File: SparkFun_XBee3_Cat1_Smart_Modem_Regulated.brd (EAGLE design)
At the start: 33 x 52.1 mm, 95 parts, among them J4 QWIIC_RIGHT_ANGLE, U2 AP63203

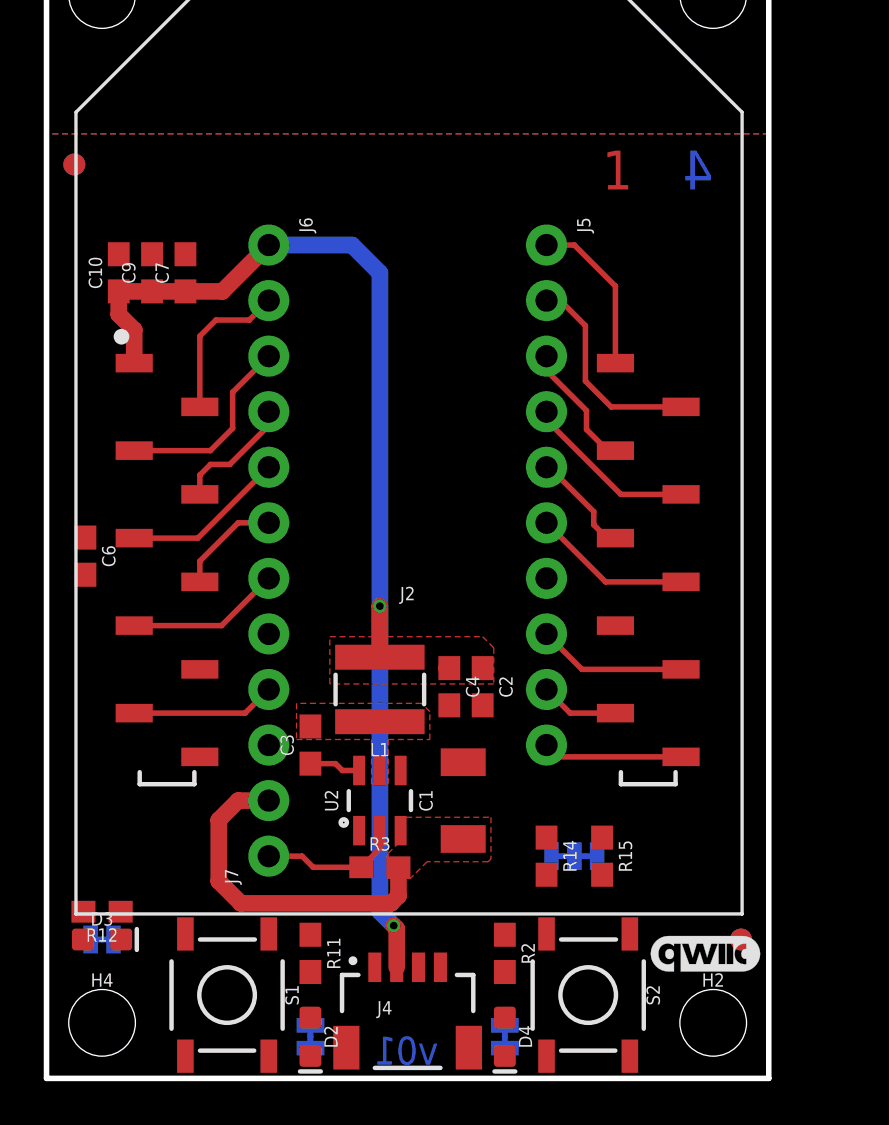
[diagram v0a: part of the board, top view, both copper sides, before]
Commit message: Routes the board (roughly)
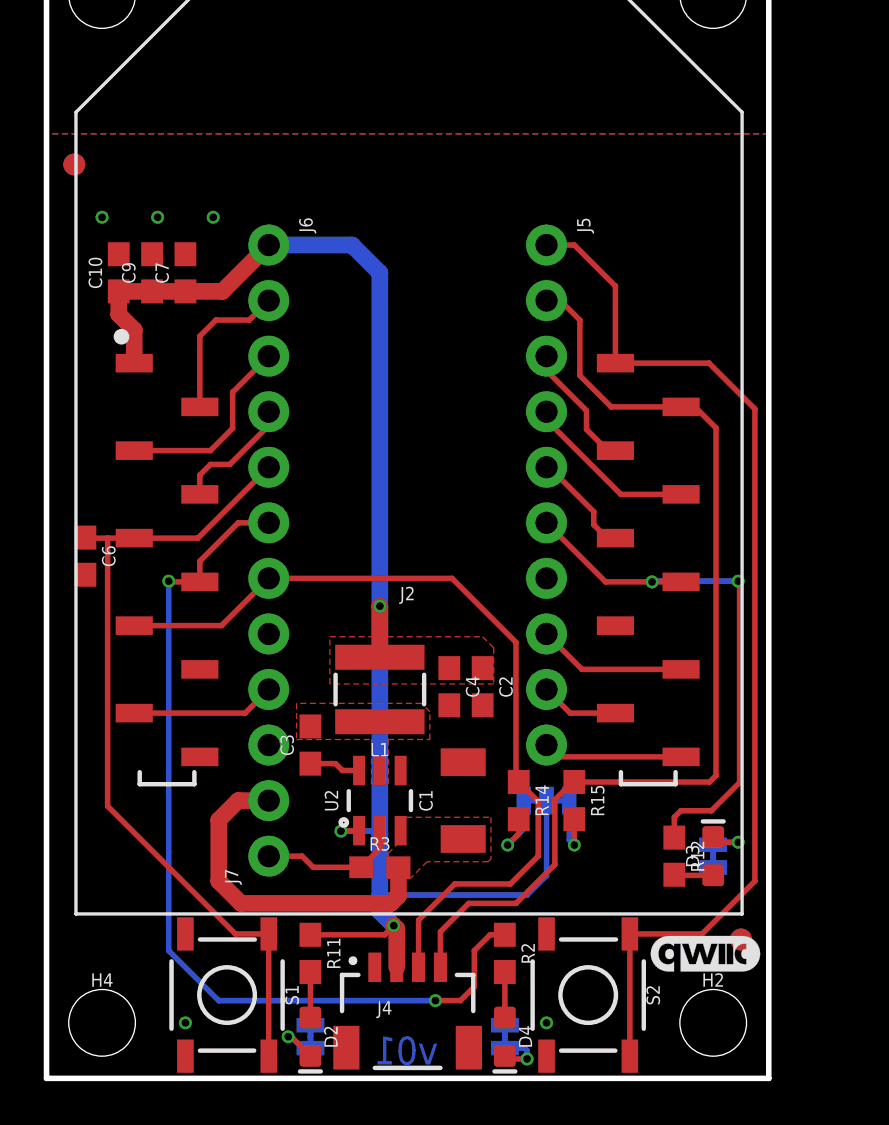
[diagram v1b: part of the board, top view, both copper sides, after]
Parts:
- moved ALED 28.2 mm to (30.5, 10.2), turned to 90 degrees
- moved D3 28.2 mm to (30.5, 10.2), turned to 90 degrees
- moved R12 26.3 mm to (28.7, 10.2), turned to 270 degrees
- moved U$13 3.59 mm to (30.0, 12.7)
- moved I2C_PU 2.84 mm to (22.9, 12.7)
- moved R14 2.84 mm to (21.6, 12.7)
- moved R15 2.84 mm to (24.1, 12.7)
- turned PLED to 270 degrees
- turned RLED to 270 degrees
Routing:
- net D0: track 7.45 -> 48.6 mm
- net D1/SCL: track 9.65 -> 46.5 mm
- net D10/RSSI_PWM: track 5.33 -> 41.7 mm, vias 0 -> 2
- net D11/SDA: track 7.04 -> 38.6 mm
- net !RESET!: track 7.49 -> 37.4 mm
- net 3.3V: track 51.5 -> 69.4 mm, vias 2 -> 3
- net D5/ASSOCIATE: track 7.27 -> 25.0 mm, vias 0 -> 2
- net N$11: track 0.00 -> 3.73 mm, vias 0 -> 1
- net N$13: track 0.00 -> 3.31 mm, vias 0 -> 1
- net N$23: track 0.00 -> 2.61 mm, vias 0 -> 1
- net N$3: track 0.00 -> 2.52 mm, vias 0 -> 1
- net N$21: track 0.00 -> 2.43 mm, vias 0 -> 1
- net N$7: track 0.00 -> 2.08 mm
- net N$2: track 0.00 -> 2.08 mm
- net N$12: track 0.00 -> 1.79 mm
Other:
- board text removed: "1"
- board text removed: "2"
- board text removed: "3"
- board text removed: "4"

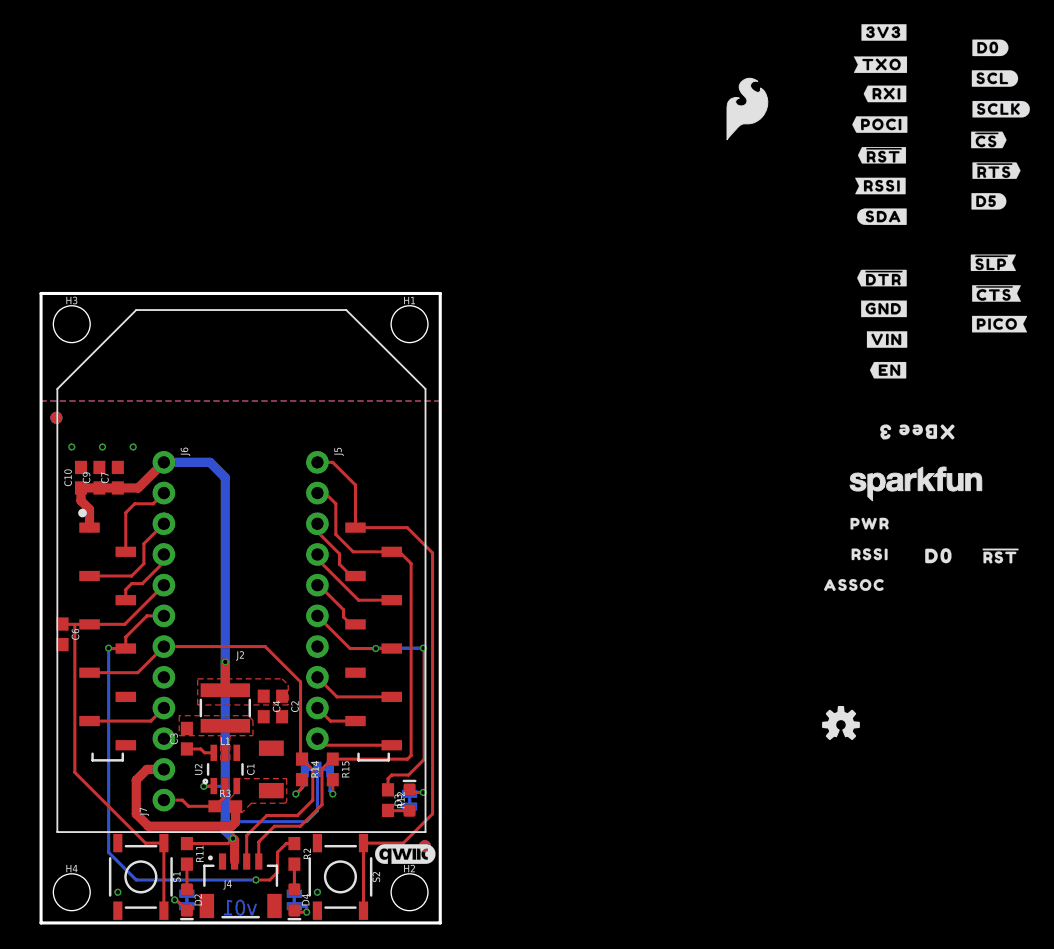
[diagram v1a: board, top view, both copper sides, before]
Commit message: Adds silk
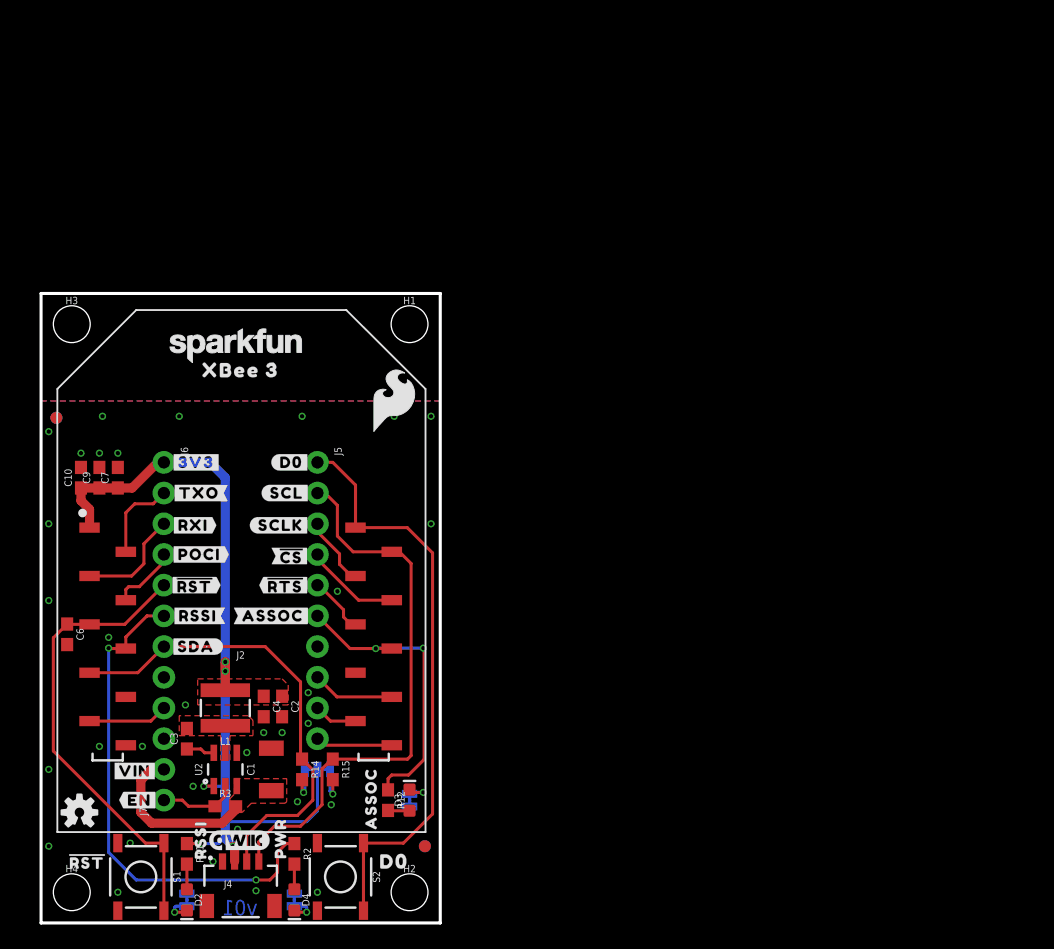
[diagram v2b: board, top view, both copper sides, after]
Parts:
- removed U$1: (no value), top:#RXI#14
- removed U$10: (no value), top:#D0#18
- removed U$2: (no value), top:##RST##15
- removed U$24: (no value), top:#EN#17
- removed U$25: (no value), top:#GND#0
- removed U$28: (no value), top:#PICO#23
- removed U$29: (no value), top:#POCI#23
- removed U$3: (no value), top:##CS##19
- removed U$31: (no value), top:#RSSI#16
- removed U$32: (no value), top:#SCL#7
- removed U$33: (no value), top:#SCLK#18
- removed U$34: (no value), top:#SDA#7
- removed U$39: (no value), bot:#D5#3
- removed U$4: (no value), top:##CTS##25
- removed U$41: (no value), top:#VIN#4
- removed U$47: (no value), top:##SLP##27
- removed U$5: (no value), top:##DTR##27
- removed U$50: (no value), top:#TXO#12
- removed U$7: (no value), top:##RTS##24
- added U$11: (no value), topmirror:#D1#AD1#8
- added U$20: (no value), topmirror:#D6##RTS##25
- added U$35: (no value), topmirror:#D5#ASSOC#25
- added U$36: (no value), topmirror:#D9##SLP##28
- added U$37: (no value), topmirror:#D7##CTS##26
- added U$38: (no value), topmirror:#D4#PICO#25
- added U$48: (no value), topmirror:#EN#17
- added U$49: (no value), topmirror:#ALED#21
- added U$51: (no value), topmirror:#RLED#22
- added U$52: (no value), topmirror:#PLED#20
- added U$65: (no value), botmirror:#D0#3
- added U$66: (no value), top:#VIN#4
- added U$67: (no value), botmirror:#EN#15
- added U$8: (no value), topmirror:#D0#AD0#18
- U$12: device top:#D3#AD3#22 -> topmirror:#GND#0
- U$13: device top:#D4#PICO#24 -> topmirror:#D8##DTR##27
- U$14: device top:#POCI#D12#24 -> topmirror:#RSSI#D10#17
- U$15: device top:#TXO#D13#13 -> topmirror:#SDA#D11#9
- U$16: device top:#RXI#D14#15 -> topmirror:##RST##15
- U$17: device top:##RST##15 -> topmirror:#POCI#D12#24
- U$18: device top:#RSSI#D10#17 -> topmirror:#RXI#D14#15
- U$19: device top:#D1#AD1#8 -> topmirror:#D2#AD2#19
- U$21: device top:#EN#17 -> botmirror:#TXO#8
- U$22: device top:#SDA#D11#8 -> topmirror:#TXO#D13#13
- U$27: device top:#ALED#21 -> botmirror:#RXI#7
- U$45: device top:#GND#0 -> botmirror:#POCI#32
- U$54: device top:#PLED#20 -> botmirror:##RST##13
- U$55: device top:#D0#AD0#18 -> topmirror:#RSSI#16
- U$56: device top:#D5#ASSOC#24 -> botmirror:#SDA#10
- U$57: device top:#D6##RTS##24 -> botmirror:#ASSOC#28
- U$58: device top:#D7##CTS##25 -> botmirror:##RTS##14
- U$59: device top:#D8##DTR##26 -> botmirror:##CS##26
- U$6: device top:#D2#AD2#19 -> topmirror:#D3#AD3#23
- U$60: device top:#D9##SLP##27 -> botmirror:#SCLK#33
- U$64: device top:#RLED#22 -> botmirror:#SCL#9
- moved U$30 79.7 mm to (3.81, 5.08)
- moved U$9 67.1 mm to (12.8, 38.1)
- moved LOGO2 63.4 mm to (3.17, 9.14)
- moved U$62 60.2 mm to (13.2, 6.86), turned to 90 degrees
- moved U$63 57.8 mm to (16.5, 45.7)
- moved LOGO1 57.4 mm to (16.1, 47.8)
- moved U$23 56.1 mm to (16.5, 45.7), turned to 0 degrees
- moved U$54 56.1 mm to (12.7, 27.9), flipped to the top
- moved U$53 55.9 mm to (16.5, 41.9)
- moved U$27 55.8 mm to (12.6, 32.9), flipped to the top, turned to 0 degrees
- moved U$42 55.3 mm to (19.8, 6.99), turned to 90 degrees
- moved U$40 51.7 mm to (29.2, 5.08)
- moved U$64 51.2 mm to (20.3, 35.6), flipped to the top, turned to 0 degrees
- moved U$45 48.1 mm to (13.1, 30.5), flipped to the top
- moved U$21 46.5 mm to (13.1, 35.6), flipped to the top
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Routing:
- net D8/!DTR!: track 13.5 -> 6.60 mm
- net VIN: track 15.5 -> 13.9 mm
- net !RESET!: track 37.4 -> 38.2 mm
- net N$11: track 3.73 -> 3.05 mm
- net 3.3V: track 69.4 -> 69.6 mm, vias 3 -> 5

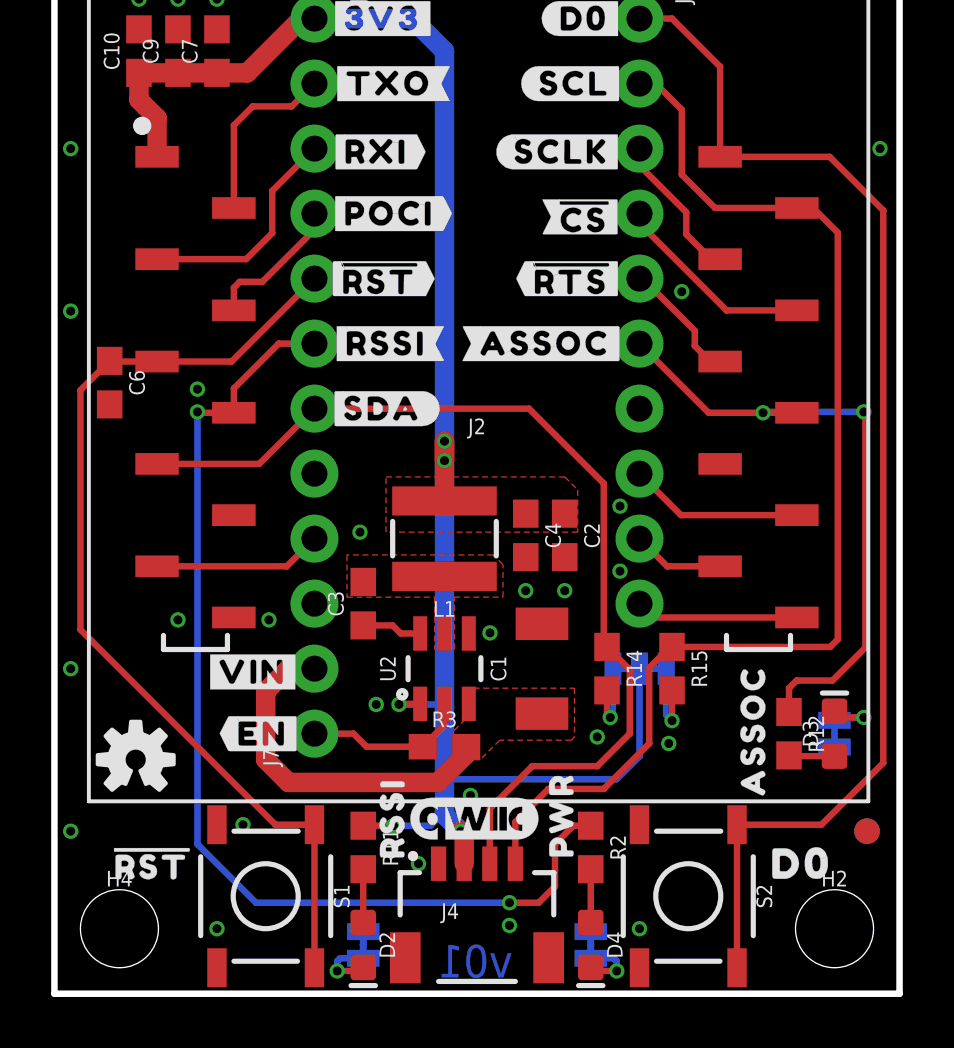
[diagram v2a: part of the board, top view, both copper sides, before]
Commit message: MOves to a smaller schematic symbol, tries to make the associate LED visible
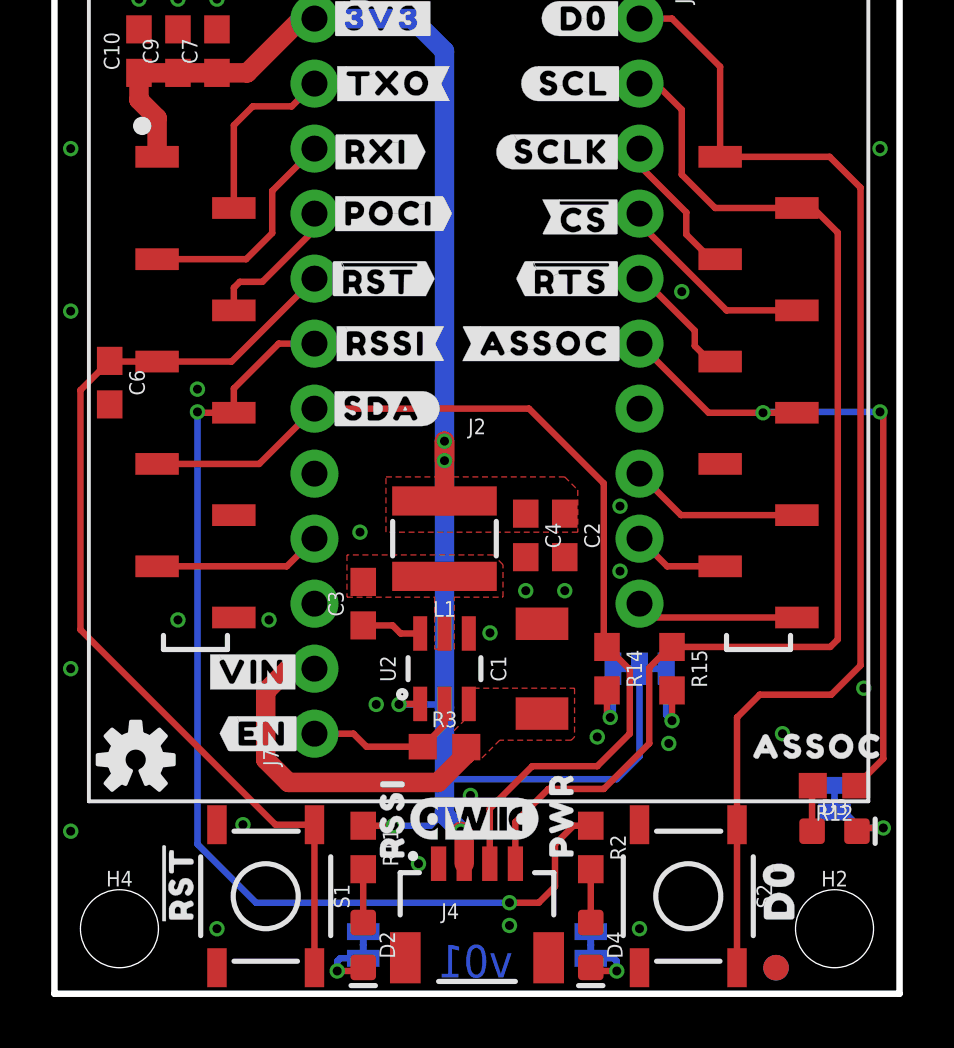
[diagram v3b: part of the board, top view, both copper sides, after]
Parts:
- removed FRAME1: FRAME-LEDGER, SparkFun-Aesthetics:CREATIVE_COMMONS
- added FRAME2: FRAME-LETTER, SparkFun-Aesthetics:CREATIVE_COMMONS
- moved FD3 6.41 mm to (28.2, 1.02)
- moved FD4 6.41 mm to (28.2, 1.02)
- moved D3 3.81 mm to (30.5, 6.35), turned to 0 degrees
- moved R12 2.70 mm to (30.5, 8.13), turned to 180 degrees
- moved U$43 2.62 mm to (29.8, 9.65), turned to 0 degrees
- moved ALED 2.54 mm to (30.5, 7.62), turned to 270 degrees
- moved U$49 2.54 mm to (27.2, 7.62)
- moved U$40 1.35 mm to (28.3, 4.06), turned to 90 degrees
- moved U$30 1.27 mm to (4.83, 4.32), turned to 90 degrees
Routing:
- net D5/ASSOCIATE: track 25.0 -> 26.9 mm
- net D0: track 48.6 -> 47.5 mm
- net N$21: track 2.43 -> 3.24 mm

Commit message: MOre vias
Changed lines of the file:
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@@
 <via x="28.448" y="10.16" extent="1-16" drill="0.35"/>
 <via x="31.623" y="11.938" extent="1-16" drill="0.35"/>
+<via x="16.51" y="26.67" extent="1-16" drill="0.35"/>
+<via x="16.51" y="34.29" extent="1-16" drill="0.35"/>
+<via x="13.97" y="34.29" extent="1-16" drill="0.35"/>
+<via x="13.97" y="26.67" extent="1-16" drill="0.35"/>
+<via x="13.97" y="21.59" extent="1-16" drill="0.35"/>
+<via x="16.51" y="21.59" extent="1-16" drill="0.35"/>
 </signal>
 <signal name="3.3V">
@@
 </polygon>
 <contactref element="J6" pad="1"/>
-<via x="15.24" y="21.59" extent="1-16" drill="0.35"/>
-<wire x1="15.24" y1="19.2532" x2="15.24" y2="21.59" width="0.762" layer="1"/>
+<via x="15.24" y="21.463" extent="1-16" drill="0.35"/>
+<wire x1="15.24" y1="19.2532" x2="15.24" y2="21.463" width="0.762" layer="1"/>
 <wire x1="15.24" y1="36.83" x2="13.97" y2="38.1" width="0.762" layer="16"/>
 <wire x1="13.97" y1="38.1" x2="10.16" y2="38.1" width="0.762" layer="16"/>
@@
 <wire x1="9.652" y1="38.1" x2="10.16" y2="38.1" width="0.762" layer="1"/>
 <wire x1="9.652" y1="38.1" x2="7.532" y2="35.98" width="0.762" layer="1"/>
-<wire x1="15.24" y1="21.59" x2="15.24" y2="11.176" width="0.762" layer="16"/>
+<wire x1="15.24" y1="21.463" x2="15.24" y2="11.176" width="0.762" layer="16"/>
 <wire x1="15.24" y1="11.176" x2="15.24" y2="8.382" width="0.762" layer="16"/>
 <wire x1="15.24" y1="8.382" x2="15.24" y2="7.112" width="0.762" layer="16"/>
@@
 <wire x1="15.24" y1="6.985" x2="15.875" y2="6.35" width="0.762" layer="16"/>
 <via x="15.875" y="6.35" extent="1-16" drill="0.35"/>
-<wire x1="15.24" y1="21.59" x2="15.24" y2="36.83" width="0.762" layer="16"/>
+<wire x1="15.24" y1="21.463" x2="15.24" y2="36.83" width="0.762" layer="16"/>
 <wire x1="22.86" y1="9.271" x2="21.971" y2="8.382" width="0.254" layer="16"/>
 <wire x1="21.971" y1="8.382" x2="15.24" y2="8.382" width="0.254" layer="16"/>
@@
 <wire x1="15.113" y1="11.303" x2="15.24" y2="11.176" width="0.254" layer="16"/>
 <via x="15.24" y="20.828" extent="1-16" drill="0.35"/>
-<wire x1="15.24" y1="20.828" x2="15.24" y2="21.59" width="0.762" layer="1"/>
+<wire x1="15.24" y1="20.828" x2="15.24" y2="21.463" width="0.762" layer="1"/>
 <wire x1="13.247" y1="6.565" x2="12.065" y2="6.565" width="0.254" layer="1"/>
 <wire x1="15.875" y1="6.35" x2="16.01" y2="6.215" width="0.762" layer="1"/>
@@
 <via x="27.686" y="22.7" extent="1-16" drill="0.35"/>
 <wire x1="31.33" y1="8.128" x2="32.385" y2="9.183" width="0.254" layer="1"/>
-<wire x1="32.385" y1="22.606" x2="32.258" y2="22.733" width="0.254" layer="1"/>
-<via x="32.258" y="22.733" extent="1-16" drill="0.35"/>
-<wire x1="32.385" y1="9.183" x2="32.385" y2="22.606" width="0.254" layer="1"/>
-<wire x1="32.258" y1="22.733" x2="27.719" y2="22.733" width="0.254" layer="16"/>
+<via x="32.385" y="22.733" extent="1-16" drill="0.35"/>
+<wire x1="32.385" y1="9.183" x2="32.385" y2="22.733" width="0.254" layer="1"/>
+<wire x1="32.385" y1="22.733" x2="27.719" y2="22.733" width="0.254" layer="16"/>
 </signal>
 <signal name="D6/!RTS!">
@@
 <wire x1="26.67" y1="1.016" x2="26.67" y2="6.604" width="0.254" layer="1"/>
 <wire x1="30.292" y1="32.7" x2="26.01" y2="32.7" width="0.254" layer="1"/>
-<wire x1="31.496" y1="31.496" x2="30.292" y2="32.7" width="0.254" layer="1"/>
+<wire x1="31.369" y1="31.623" x2="30.292" y2="32.7" width="0.254" layer="1"/>
 <wire x1="26.67" y1="6.604" x2="26.67" y2="10.795" width="0.254" layer="1"/>
 <wire x1="27.559" y1="11.684" x2="30.353" y2="11.684" width="0.254" layer="1"/>
-<wire x1="30.353" y1="11.684" x2="31.496" y2="12.827" width="0.254" layer="1"/>
-<wire x1="31.496" y1="12.827" x2="31.496" y2="31.496" width="0.254" layer="1"/>
+<wire x1="30.353" y1="11.684" x2="31.369" y2="12.7" width="0.254" layer="1"/>
+<wire x1="31.369" y1="12.7" x2="31.369" y2="31.623" width="0.254" layer="1"/>
 <wire x1="26.67" y1="10.795" x2="27.559" y2="11.684" width="0.254" layer="1"/>
 </signal>
